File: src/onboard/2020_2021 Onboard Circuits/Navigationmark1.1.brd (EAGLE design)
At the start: 72.1 x 68.6 mm, 44 parts, among them IC1 A5975D, IC2 A5975D, IC3 CD74AC257M96

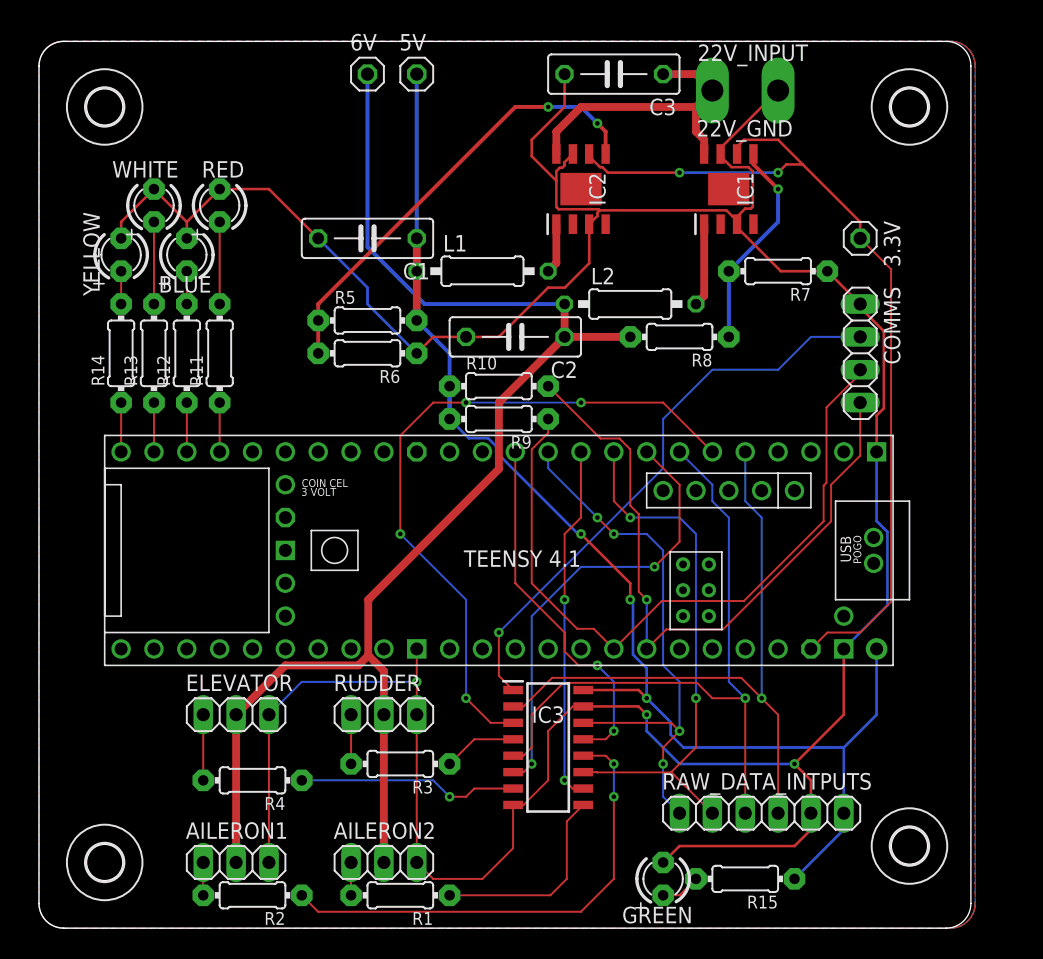
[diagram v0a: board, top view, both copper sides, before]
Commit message: Updated board using the jlcpcb2layer.dru file for DRC check. Added names next to pinheaders. Adjusted silkscreen of component names. Updated photos of baord and schematic.
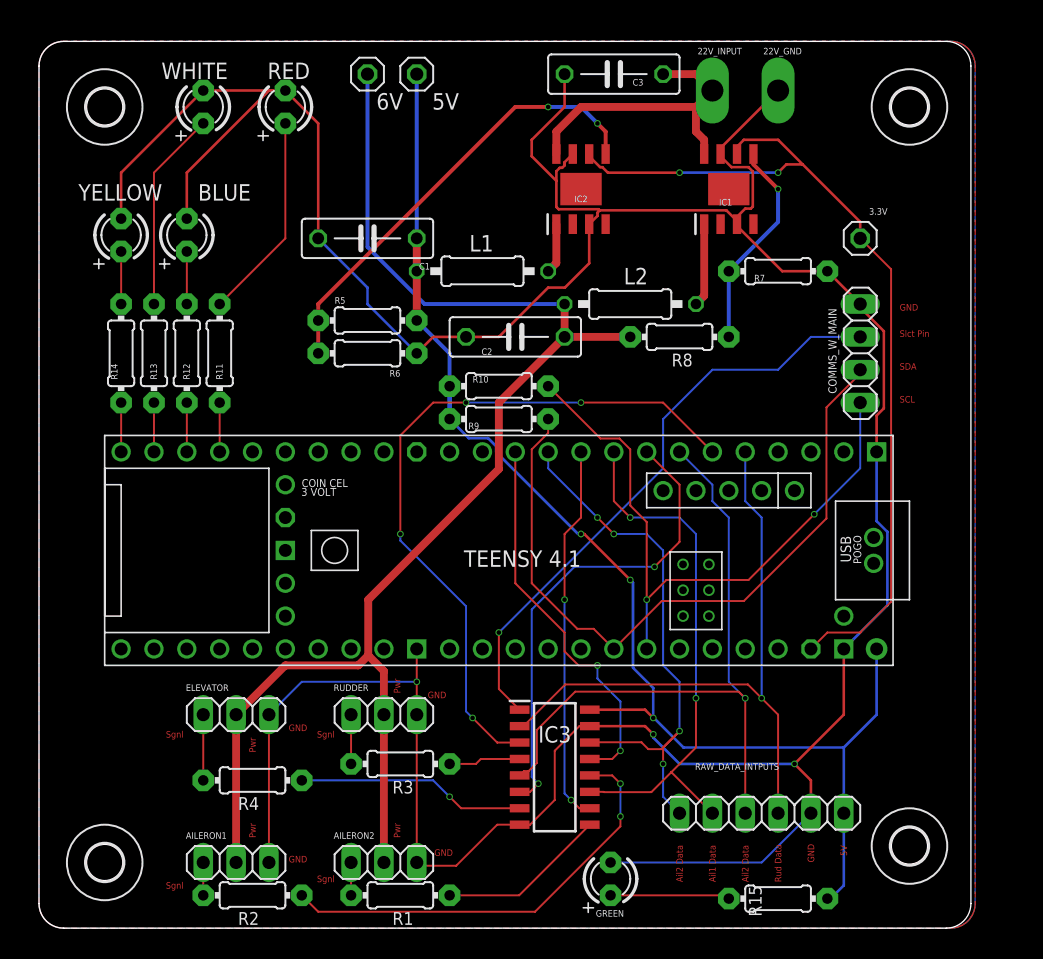
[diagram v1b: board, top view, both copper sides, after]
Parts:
- moved RED 9.16 mm to (52.1, 73.7)
- moved WHITE 8.52 mm to (45.7, 73.7)
- moved GREEN 4.06 mm to (77.2, 14.0)
- moved R15 2.96 mm to (90.2, 12.4)
- moved IC3 1.61 mm to (72.9, 22.6)
- moved BLUE 1.52 mm to (44.5, 63.8)
- moved YELLOW 1.52 mm to (39.4, 63.8)
- renumbered COMMS to COMMS_W_MAIN
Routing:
- net GND: track 252.4 -> 273.3 mm
- net N$9: track 6.35 -> 16.1 mm
- net N$16: track 6.35 -> 15.5 mm
- net N$2: track 3.07 -> 9.25 mm
- net AILERON1_SIGNAL: track 37.2 -> 33.8 mm
- net AILERON2_SIGNAL: track 15.8 -> 13.1 mm
- net SCL: track 52.8 -> 50.1 mm, vias 1 -> 2
- net FILTERED_ELEV: track 35.0 -> 37.0 mm
- net SELECT_PIN: track 44.5 -> 46.3 mm
- net FILTERED_RUD: track 53.6 -> 55.3 mm
- net FILTERED_AILERON2: track 28.2 -> 30.0 mm
- net FILTERED_AILERON1: track 27.6 -> 29.4 mm
- net N$17: track 2.54 -> 4.06 mm
- net N$15: track 2.54 -> 4.06 mm
- net RAW_AILERON2_DATA: track 42.4 -> 43.3 mm
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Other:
- board text added: "5V"
- board text added: "Ail1 Data"
- board text added: "Ail2 Data"
- board text added: "GND"
- board text added: "Pwr"
- board text added: "Rud Data"
- board text added: "SCL"
- board text added: "SDA"
- board text added: "Sgnl"
- board text added: "Slct Pin"

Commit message: Changed Pinheader side names to Tplace on both boards
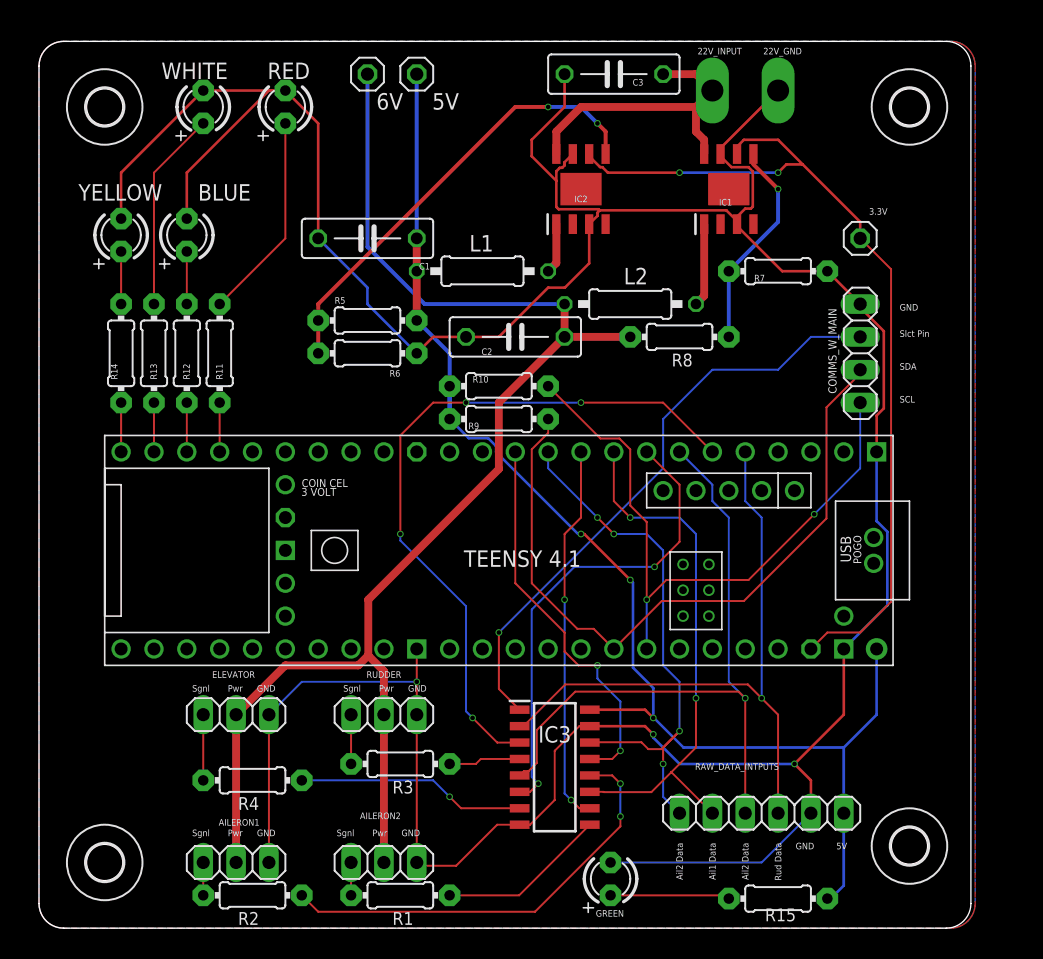
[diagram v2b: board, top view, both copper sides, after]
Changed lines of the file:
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@@
 <wire x1="105.08" y1="12.065" x2="105.08" y2="76.825" width="0" layer="20"/>
 <wire x1="105.08" y1="76.825" x2="103.175" y2="78.73" width="0" layer="20" curve="90"/>
-<text x="99.568" y="57.912" size="0.508" layer="1" font="vector">GND</text>
-<text x="99.568" y="55.88" size="0.508" layer="1" font="vector">Slct Pin</text>
-<text x="99.568" y="53.34" size="0.508" layer="1" font="vector">SDA</text>
-<text x="99.568" y="50.8" size="0.508" layer="1" font="vector">SCL</text>
-<text x="82.804" y="13.716" size="0.508" layer="1" font="vector" rot="R90">Ail2 Data</text>
-<text x="85.344" y="13.716" size="0.508" layer="1" font="vector" rot="R90">Ail1 Data</text>
-<text x="87.884" y="13.716" size="0.508" layer="1" font="vector" rot="R90">Ail2 Data</text>
-<text x="90.424" y="13.716" size="0.508" layer="1" font="vector" rot="R90">Rud Data</text>
-<text x="92.964" y="15.24" size="0.508" layer="1" font="vector" rot="R90">GND</text>
-<text x="95.504" y="15.748" size="0.508" layer="1" font="vector" rot="R90">5V</text>
-<text x="65.024" y="16.256" size="0.508" layer="1" font="vector" rot="R180">GND</text>
-<text x="64.516" y="28.448" size="0.508" layer="1" font="vector" rot="R180">GND</text>
-<text x="52.324" y="25.4" size="0.508" layer="1" font="vector">GND</text>
-<text x="52.324" y="15.24" size="0.508" layer="1" font="vector">GND</text>
-<text x="44.196" y="13.716" size="0.508" layer="1" font="vector" rot="R180">Sgnl</text>
-<text x="44.196" y="25.4" size="0.508" layer="1" font="vector" rot="R180">Sgnl</text>
-<text x="55.88" y="25.4" size="0.508" layer="1" font="vector" rot="R180">Sgnl</text>
-<text x="55.88" y="14.224" size="0.508" layer="1" font="vector" rot="R180">Sgnl</text>
-<text x="49.276" y="24.892" size="0.508" layer="1" font="vector" rot="R270">Pwr</text>
-<text x="49.276" y="18.288" size="0.508" layer="1" font="vector" rot="R270">Pwr</text>
-<text x="60.452" y="18.288" size="0.508" layer="1" font="vector" rot="R270">Pwr</text>
-<text x="60.452" y="29.464" size="0.508" layer="1" font="vector" rot="R270">Pwr</text>
+<text x="99.568" y="57.912" size="0.508" layer="21" font="vector">GND</text>
+<text x="99.568" y="55.88" size="0.508" layer="21" font="vector">Slct Pin</text>
+<text x="99.568" y="53.34" size="0.508" layer="21" font="vector">SDA</text>
+<text x="99.568" y="50.8" size="0.508" layer="21" font="vector">SCL</text>
+<text x="82.296" y="16.764" size="0.508" layer="21" font="vector" rot="R270">Ail2 Data</text>
+<text x="84.836" y="16.764" size="0.508" layer="21" font="vector" rot="R270">Ail1 Data</text>
+<text x="87.376" y="16.764" size="0.508" layer="21" font="vector" rot="R270">Ail2 Data</text>
+<text x="89.916" y="16.764" size="0.508" layer="21" font="vector" rot="R270">Rud Data</text>
+<text x="92.964" y="16.764" size="0.508" layer="21" font="vector" rot="R180">GND</text>
+<text x="95.504" y="16.764" size="0.508" layer="21" font="vector" rot="R180">5V</text>
+<text x="62.484" y="17.78" size="0.508" layer="21" font="vector" rot="R180">GND</text>
+<text x="62.992" y="28.956" size="0.508" layer="21" font="vector" rot="R180">GND</text>
+<text x="51.308" y="28.956" size="0.508" layer="21" font="vector" rot="R180">GND</text>
+<text x="51.308" y="17.78" size="0.508" layer="21" font="vector" rot="R180">GND</text>
+<text x="46.228" y="17.78" size="0.508" layer="21" font="vector" rot="R180">Sgnl</text>
+<text x="46.228" y="28.956" size="0.508" layer="21" font="vector" rot="R180">Sgnl</text>
+<text x="57.912" y="28.956" size="0.508" layer="21" font="vector" rot="R180">Sgnl</text>
+<text x="57.404" y="17.78" size="0.508" layer="21" font="vector" rot="R180">Sgnl</text>
+<text x="48.768" y="28.956" size="0.508" layer="21" font="vector" rot="R180">Pwr</text>
+<text x="48.768" y="17.78" size="0.508" layer="21" font="vector" rot="R180">Pwr</text>
+<text x="59.944" y="17.78" size="0.508" layer="21" font="vector" rot="R180">Pwr</text>
+<text x="60.452" y="28.956" size="0.508" layer="21" font="vector" rot="R180">Pwr</text>
 </plain>
 <attributes>
@@
 </element>
 <element name="AILERON1" library="pinhead" library_urn="urn:adsk.eagle:library:325" package="1X03" package3d_urn="urn:adsk.eagle:package:22458/2" value="" x="48.26" y="15.24" smashed="yes">
-<attribute name="NAME" x="44.3738" y="17.0688" size="0.508" layer="25" ratio="10"/>
+<attribute name="NAME" x="46.9138" y="18.0848" size="0.508" layer="25" ratio="10"/>
 <attribute name="POPULARITY" value="92" x="109.22" y="-17.78" size="1.778" layer="27" display="off"/>
 <attribute name="VALUE" x="44.45" y="12.065" size="1.27" layer="27"/>
 </element>
 <element name="AILERON2" library="pinhead" library_urn="urn:adsk.eagle:library:325" package="1X03" package3d_urn="urn:adsk.eagle:package:22458/2" value="" x="59.69" y="15.24" smashed="yes">
-<attribute name="NAME" x="55.8038" y="17.0688" size="0.508" layer="25" ratio="10"/>
+<attribute name="NAME" x="57.8358" y="18.5928" size="0.508" layer="25" ratio="10"/>
 <attribute name="POPULARITY" value="92" x="78.74" y="-24.13" size="1.778" layer="27" display="off"/>
 <attribute name="VALUE" x="55.88" y="12.065" size="1.27" layer="27"/>
@@
 </element>
 <element name="ELEVATOR" library="pinhead" library_urn="urn:adsk.eagle:library:325" package="1X03" package3d_urn="urn:adsk.eagle:package:22458/2" value="" x="48.26" y="26.67" smashed="yes">
-<attribute name="NAME" x="44.3738" y="28.4988" size="0.508" layer="25" ratio="10"/>
+<attribute name="NAME" x="46.4058" y="29.5148" size="0.508" layer="25" ratio="10"/>
 <attribute name="POPULARITY" value="92" x="99.06" y="-6.35" size="1.778" layer="27" display="off"/>
 <attribute name="VALUE" x="44.45" y="23.495" size="1.27" layer="27"/>
@@
 </element>
 <element name="RUDDER" library="pinhead" library_urn="urn:adsk.eagle:library:325" package="1X03" package3d_urn="urn:adsk.eagle:package:22458/2" value="" x="59.69" y="26.67" smashed="yes">
-<attribute name="NAME" x="55.8038" y="28.4988" size="0.508" layer="25" ratio="10"/>
+<attribute name="NAME" x="58.3438" y="29.5148" size="0.508" layer="25" ratio="10"/>
 <attribute name="POPULARITY" value="92" x="87.63" y="-12.7" size="1.778" layer="27" display="off"/>
 <attribute name="VALUE" x="55.88" y="23.495" size="1.27" layer="27"/>
@@
 </element>
 <element name="R15" library="adafruit" library_urn="urn:adsk.eagle:library:420" package="0204/7" package3d_urn="urn:adsk.eagle:package:6240596/1" value="150" x="90.17" y="12.446" smashed="yes" rot="R180">
-<attribute name="NAME" x="87.9094" y="13.462" size="0.9906" layer="25" ratio="12" rot="R270"/>
+<attribute name="NAME" x="89.154" y="10.6934" size="0.9906" layer="25" ratio="12"/>
 <attribute name="VALUE" x="91.7956" y="12.9286" size="0.9906" layer="27" ratio="12" rot="R180"/>
 </element>

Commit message: Removed 5V lines as one layer is a 5V pour so they were not needed because the components are through hole. Then updated photos of both boards
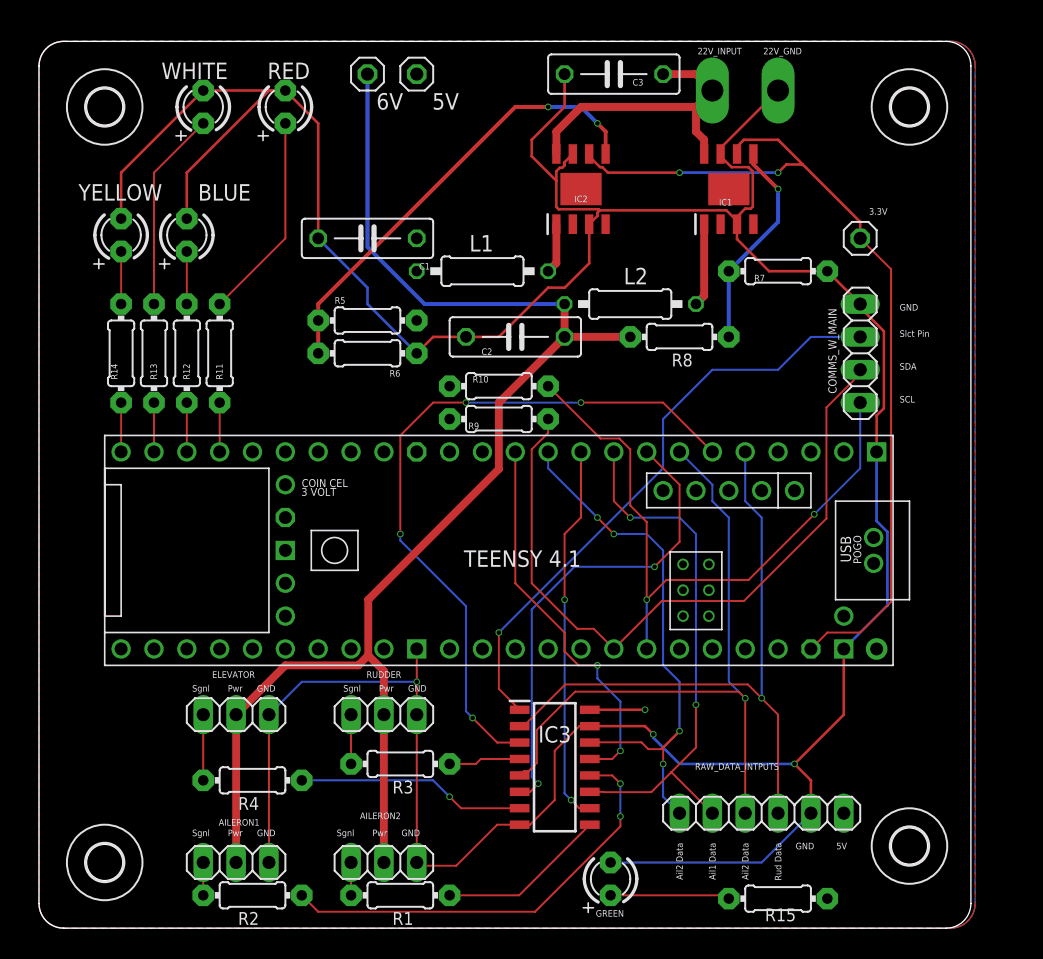
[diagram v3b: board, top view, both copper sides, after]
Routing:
- net 5V: track 102.9 -> 4.27 mm, vias 3 -> 1
- net GND: track 273.3 -> 273.9 mm
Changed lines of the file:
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@@
 <wire x1="87.8787125" y1="69.0055" x2="86.5647875" y2="69.0055" width="0.2032" layer="1"/>
 <wire x1="88.214" y1="65.9497875" x2="88.214" y2="68.6702125" width="0.2032" layer="1"/>
-<wire x1="93.98" y1="60.96" x2="90.4922125" y2="60.96" width="0.2032" layer="1"/>
+<wire x1="93.98" y1="60.96" x2="89.4762125" y2="60.96" width="0.2032" layer="1"/>
 <wire x1="93.98" y1="60.96" x2="96.52" y2="58.42" width="0.2032" layer="1"/>
 <wire x1="87.63" y1="65.801" x2="88.0652125" y2="65.801" width="0.2032" layer="1"/>
@@
 <wire x1="86.995" y1="64.598" x2="86.995" y2="65.166" width="0.2032" layer="1"/>
 <wire x1="86.995" y1="65.166" x2="87.63" y2="65.801" width="0.2032" layer="1"/>
-<wire x1="90.4922125" y1="60.96" x2="86.995" y2="64.4572125" width="0.2032" layer="1"/>
-<wire x1="86.995" y1="64.598" x2="86.995" y2="64.4572125" width="0.2032" layer="1"/>
+<wire x1="89.4762125" y1="60.96" x2="86.995" y2="63.4412125" width="0.2032" layer="1"/>
+<wire x1="86.995" y1="64.598" x2="86.995" y2="63.4412125" width="0.2032" layer="1"/>
 </signal>
 <signal name="SELECT_PIN">
@@
 <wire x1="78.74" y1="41.91" x2="77.47" y2="43.18" width="0.1524" layer="1"/>
 <wire x1="77.47" y1="43.18" x2="77.47" y2="46.99" width="0.1524" layer="1"/>
-<wire x1="83.82" y1="40.64" x2="83.82" y2="27.94" width="0.1524" layer="16"/>
+<wire x1="83.82" y1="40.64" x2="83.82" y2="27.432" width="0.1524" layer="16"/>
 <wire x1="82.55" y1="41.91" x2="78.74" y2="41.91" width="0.1524" layer="16"/>
 <contactref element="RAW_DATA_INTPUTS" pad="2"/>
-<via x="83.82" y="27.94" extent="1-16" drill="0.35"/>
-<wire x1="83.82" y1="27.94" x2="83.82" y2="24.13" width="0.1524" layer="1"/>
+<via x="83.82" y="27.432" extent="1-16" drill="0.35"/>
+<wire x1="83.82" y1="27.432" x2="83.82" y2="24.13" width="0.1524" layer="1"/>
 <wire x1="85.09" y1="19.05" x2="81.915" y2="22.225" width="0.1524" layer="1"/>
 <wire x1="83.82" y1="24.13" x2="81.915" y2="22.225" width="0.1524" layer="1"/>
@@
 <contactref element="R10" pad="1"/>
 <contactref element="IC3" pad="16"/>
-<wire x1="62.23" y1="60.96" x2="62.23" y2="63.5" width="0.6096" layer="1"/>
-<wire x1="62.23" y1="60.96" x2="62.23" y2="57.15" width="0.6096" layer="1"/>
-<wire x1="62.23" y1="63.5" x2="62.23" y2="76.2" width="0.3048" layer="16"/>
-<wire x1="62.23" y1="57.15" x2="64.77" y2="54.61" width="0.3048" layer="16"/>
-<wire x1="64.77" y1="54.61" x2="64.77" y2="49.53" width="0.3048" layer="16"/>
-<wire x1="64.77" y1="49.53" x2="64.77" y2="52.07" width="0.3048" layer="16"/>
-<via x="80.518" y="26.416" extent="1-16" drill="0.35"/>
-<via x="78.74" y="37.084" extent="1-16" drill="0.35"/>
-<via x="74.93" y="40.64" extent="1-16" drill="0.35"/>
 <contactref element="R15" pad="1"/>
 <contactref element="RAW_DATA_INTPUTS" pad="6"/>
@@
 <vertex x="105.41" y="76.835" curve="90"/>
 </polygon>
-<wire x1="67.748575" y1="48.0488" x2="68.3688" y2="47.428575" width="0.2032" layer="16"/>
-<wire x1="64.77" y1="49.53" x2="66.2512" y2="48.0488" width="0.2032" layer="16"/>
-<wire x1="66.2512" y1="48.0488" x2="67.748575" y2="48.0488" width="0.2032" layer="16"/>
-<wire x1="68.3688" y1="47.428575" x2="68.3688" y2="46.973825" width="0.2032" layer="16"/>
-<wire x1="68.3688" y1="46.973825" x2="74.702625" y2="40.64" width="0.2032" layer="16"/>
-<wire x1="74.702625" y1="40.64" x2="74.93" y2="40.64" width="0.2032" layer="16"/>
-<wire x1="74.93" y1="40.64" x2="75.184" y2="40.64" width="0.2032" layer="1"/>
-<wire x1="75.184" y1="40.64" x2="78.74" y2="37.084" width="0.2032" layer="1"/>
-<wire x1="80.518" y1="28.728625" x2="80.518" y2="26.416" width="0.2032" layer="16"/>
-<wire x1="78.9512" y1="30.295425" x2="80.518" y2="28.728625" width="0.2032" layer="16"/>
-<wire x1="78.74" y1="37.084" x2="78.9512" y2="36.8728" width="0.2032" layer="16"/>
-<wire x1="78.9512" y1="36.8728" x2="78.9512" y2="30.295425" width="0.2032" layer="16"/>
-<wire x1="80.518" y1="26.416" x2="80.5680875" y2="26.416" width="0.2032" layer="16"/>
-<wire x1="82.8540875" y1="24.13" x2="80.5680875" y2="26.416" width="0.2032" layer="16"/>
-<wire x1="82.8540875" y1="24.13" x2="95.25" y2="24.13" width="0.2032" layer="16"/>
-<wire x1="95.25" y1="24.13" x2="95.25" y2="19.05" width="0.2032" layer="16"/>
-<wire x1="97.79" y1="31.75" x2="97.79" y2="26.67" width="0.2032" layer="16"/>
-<wire x1="97.79" y1="26.67" x2="95.25" y2="24.13" width="0.2032" layer="16"/>
-<wire x1="95.25" y1="19.05" x2="95.25" y2="13.462" width="0.2032" layer="16"/>
-<wire x1="95.25" y1="13.462" x2="94.234" y2="12.446" width="0.2032" layer="16"/>
-<wire x1="93.98" y1="12.446" x2="94.234" y2="12.446" width="0.2032" layer="16"/>
-<wire x1="80.518" y1="26.416" x2="79.883" y2="27.051" width="0.2032" layer="1"/>
+<via x="79.883" y="27.051" extent="1-16" drill="0.35"/>
 <wire x1="79.883" y1="27.051" x2="75.61" y2="27.051" width="0.2032" layer="1"/>
+<wire x1="62.23" y1="63.5" x2="62.23" y2="76.2" width="0" layer="19" extent="1-1"/>
+<wire x1="62.23" y1="60.96" x2="62.23" y2="63.5" width="0" layer="19" extent="1-1"/>
+<wire x1="62.23" y1="57.15" x2="62.23" y2="60.96" width="0" layer="19" extent="1-1"/>
+<wire x1="64.77" y1="52.07" x2="62.23" y2="57.15" width="0" layer="19" extent="1-1"/>
+<wire x1="64.77" y1="49.53" x2="64.77" y2="52.07" width="0" layer="19" extent="1-1"/>
+<wire x1="75.61" y1="27.051" x2="64.77" y2="49.53" width="0" layer="19" extent="1-1"/>
+<wire x1="95.25" y1="19.05" x2="79.883" y2="27.051" width="0" layer="19" extent="1-1"/>
+<wire x1="93.98" y1="12.446" x2="95.25" y2="19.05" width="0" layer="19" extent="1-1"/>
+<wire x1="97.79" y1="31.75" x2="95.25" y2="19.05" width="0" layer="19" extent="1-1"/>
 </signal>
 <signal name="22V">
